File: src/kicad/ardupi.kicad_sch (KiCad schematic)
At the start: 64 parts, among them J1 RPI-4B-Header, J10 Conn_01x04, J11 TSW-108-08-L-T-RA, J2 Conn_01x10, J3 Conn_01x05, J4 Conn_01x04, J6 Conn_01x05, J7 Conn_01x06, J8 Conn_01x04, J9 Conn_01x02, U1 CAT24C256HU4IGT3, U2 ULN2803ADWR, U3 PCA9685PW, U4 ADS1115IDGSR, U5 MPU-9250, U6 BMP280

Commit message: add CAT24C32WI-GT3
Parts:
- removed JP2: ID_WP, Ardupi:SOLDERJUMPER_REFLOW_NOPASTE, symbol Jumper:SolderJumper_2_Open
- removed U1: CAT24C256HU4IGT3, Ardupi:CAT24C256HU4IGT3, symbol ArduPi:CAT24C256HU4IGT3
- added R3: 1k, Resistor_SMD:R_0402_1005Metric, symbol Device:R_Small
- added SJ_A7: SOLDERJUMPERREFLOW_NOPASTE, Ardupi:SOLDERJUMPER_REFLOW_NOPASTE, symbol ArduPi:SOLDERJUMPERREFLOW_NOPASTE
- added U1: CAT24C32WI-GT3, Ardupi:CAT24C32WI-GT3, symbol ArduPi:CAT24C32WI-GT3
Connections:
- net ID_SDA is gone; now on net ID_SD: R21.1
- net +3V3: now also J1.1 (+3.3V), J1.17 (+3.3V), R3.2, U1.8 (VCC)
- net GND: now also J1.25 (GND), J1.39 (GND), J1.9 (GND), SJ_A7.1, U1.1 (A0), U1.2 (A1), U1.3 (A2), U1.4 (VSS)
- net LED1: now also J1.13 (GPIO27)
- net LED2: now also J1.15 (GPIO22)
- net LED3: now also J1.7 (GPIO4)
- net RC1: now also J1.29 (GPIO5)
- net RC2: now also J1.31 (GPIO6)
- net RC3: now also J1.33 (GPIO13)
- net RC4: now also J1.35 (GPIO_19)
- net RC5: now also J1.37 (GPIO26)
- net SCL1: now also J1.5 (GPIO3)
- net SDA1: now also J1.3 (GPIO2)
- net SPI_MISO: now also J1.21 (GPIO9)
- net SPI_MOSI: now also J1.19 (GPIO10)
- net SPI_SCLK: now also J1.23 (GPIO11)
- net SRVO_EN: now also J1.11 (GPIO17)
- net ID_SD: now reaches J1.27 (Reserved)
- net ID_SD: now also U1.5 (SDA)
- net ID_SCL renamed ID_SC
- net ID_SC: now also U1.6 (SCL)
- new net: R3.1, SJ_A7.2, U1.7 (WP)
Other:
- moved on the sheet: C4, C5, C9, C_PCA1, J1, J10, J11, J2, J3, J4, J6, J7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

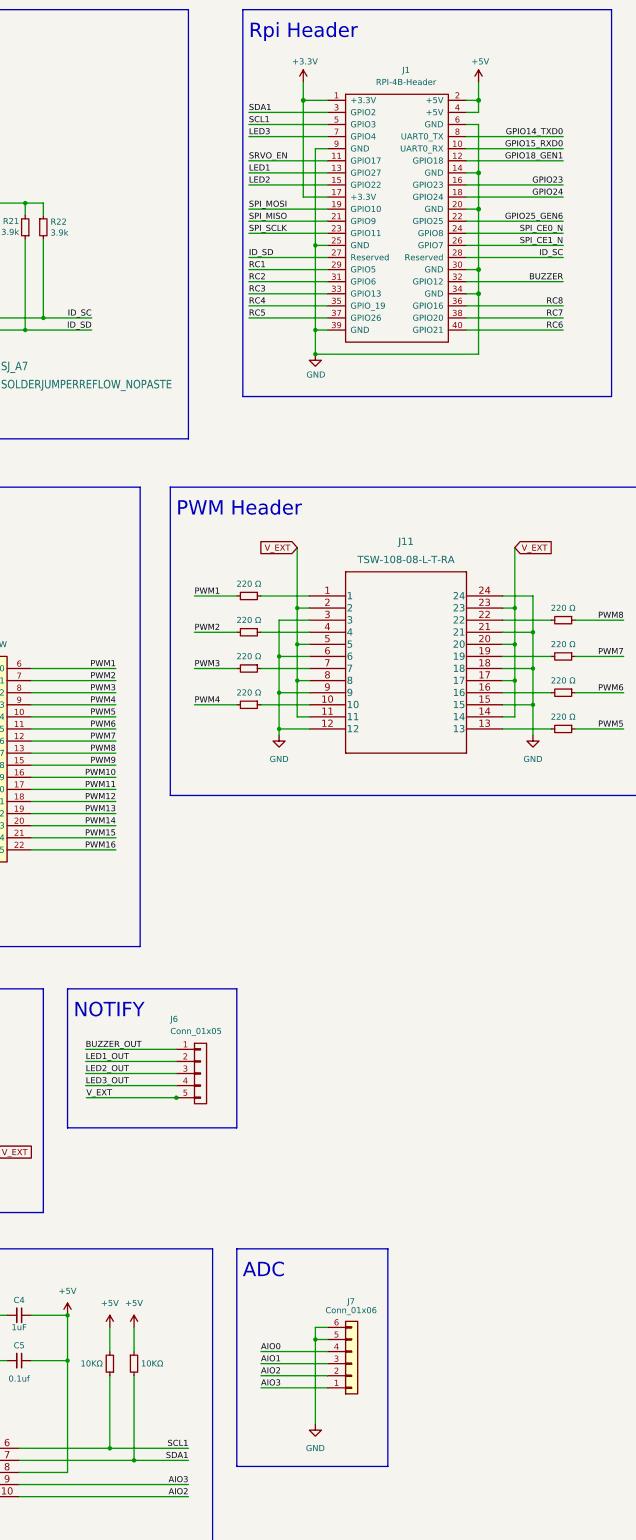
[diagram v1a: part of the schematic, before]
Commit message: define PWM header pin table.
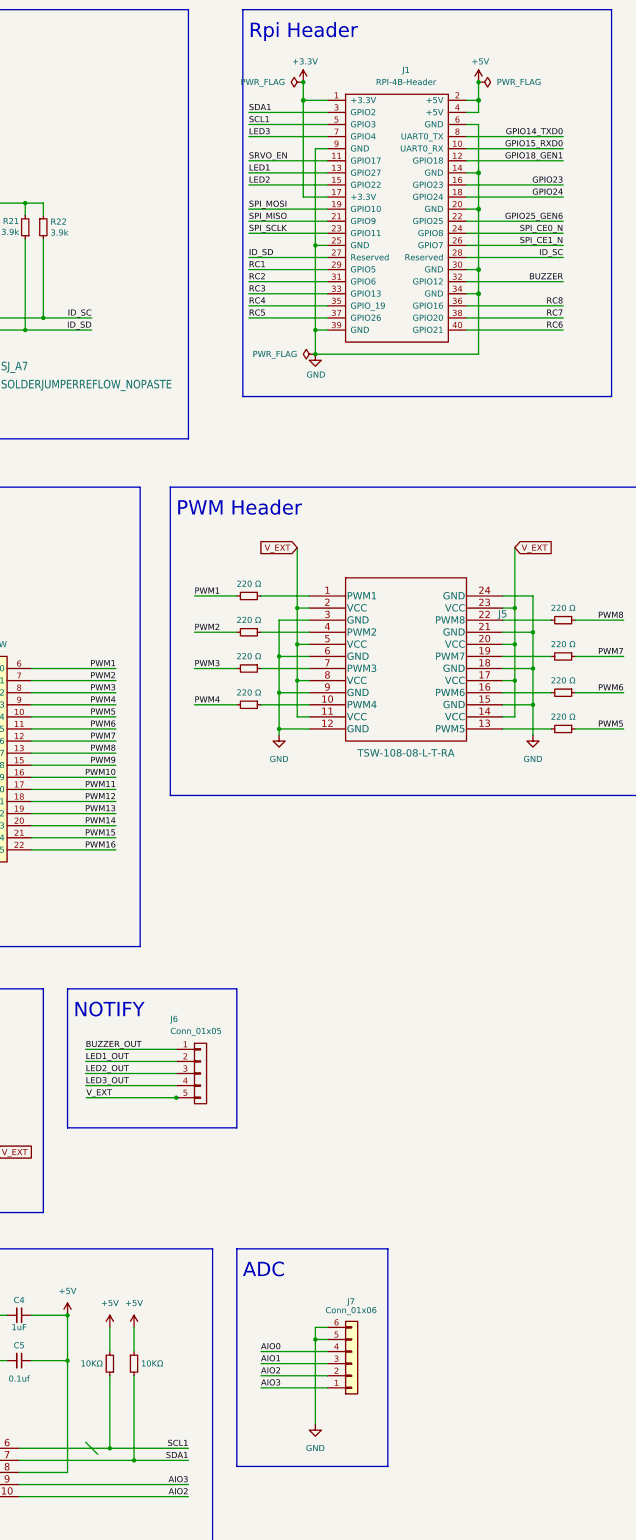
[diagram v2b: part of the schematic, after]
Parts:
- removed J11: TSW-108-08-L-T-RA, Ardupi:TSW-108-08-L-T-RA, symbol ardupi:TSW-108-08-L-T-RA
- added J5: TSW-108-08-L-T-RA, TSW-108-08-T-T-RA_SAI, symbol ArduPi:TSW-108-08-L-T-RA
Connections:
- net GND: now also J5.12 (GND), J5.15 (GND), J5.18 (GND), J5.21 (GND), J5.24 (GND), J5.3 (GND), J5.6 (GND), J5.9 (GND)
- net V_EXT: now also J5.11 (VCC), J5.14 (VCC), J5.17 (VCC), J5.2 (VCC), J5.20 (VCC), J5.23 (VCC), J5.5 (VCC), J5.8 (VCC)
- net at R20.2: now also J5.13 (PWM5)
- net at R14.1: now also J5.4 (PWM2)
- net at R16.1: now also J5.10 (PWM4)
- net at R19.2: now also J5.16 (PWM6)
- net at R18.2: now also J5.19 (PWM7)
- net at R13.1: now also J5.1 (PWM1)
- net at R17.2: now also J5.22 (PWM8)
- net at R15.1: now also J5.7 (PWM3)

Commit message: +NEO-M8Q-01A module
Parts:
- removed J10: Conn_01x04, Connector_JST:JST_EH_B4B-EH-A_1x04_P2.50mm_Vertical, symbol Connector_Generic:Conn_01x04
- added M1: NEO-M8Q-01A, Ardupi:ublox_NEO, symbol ArduPi:NEO-M8Q-01A
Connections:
- net GND: now also M1.10 (GND), M1.12 (GND), M1.13 (GND), M1.24 (GND)
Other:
- note added: "GPS"
- note removed: "COMPASS"

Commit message: + expresslrs.
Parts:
- added U7: RFM95W-868S2, Ardupi:RFM95W-868S2, symbol ArduPi:RFM95W-868S2
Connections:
- net +3V3: now also U7.13 (3_3V)
- net GND: now also U7.1 (GND), U7.10 (GND@2), U7.8 (GND@1)
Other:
- note added: "Barometer"
- note added: "ExpressLRS"
- note added: "ExpressLRS Antenna"
- note added: "GPS Antenna"
- note added: "IMU"
- note added: "LED,Buzzer"
- note added: "PWM"
- note added: "RPI Header"
- note removed: "ADS1115IDGSR ADC"
- note removed: "BMP280 Barometer"
- note removed: "ID_SD and ID_SC PINS: These pins are reserved for HAT ID EEPROM. At boot time this I2C interface will be interrogated to look for an EEPROM that identifes the attached board and allows automagic setup of the GPIOs (and optionally, Linux drivers). Bridging JP1 enables write protection. DO NOT USE these pins for anything other than attaching an I2C ID EEPROM. Leave unconnected if ID EEPROM not requ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"
- note removed: "MPU9250 IMU"
- note removed: "PCA9685 PWM"
- note removed: "Rpi Header"
- note removed: "ULN2803 LED,BUZZER"
- moved on the sheet: C2, C3, C4, C5, C6, C7, C8, C9, C_PCA1, J1, J2, J3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

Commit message: fix
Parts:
- renumbered U7 to M2
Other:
- note added: "Power Manangement"
- moved on the sheet: C2, C3, C6, C7, C8, J9, R11, R12, U5, U6

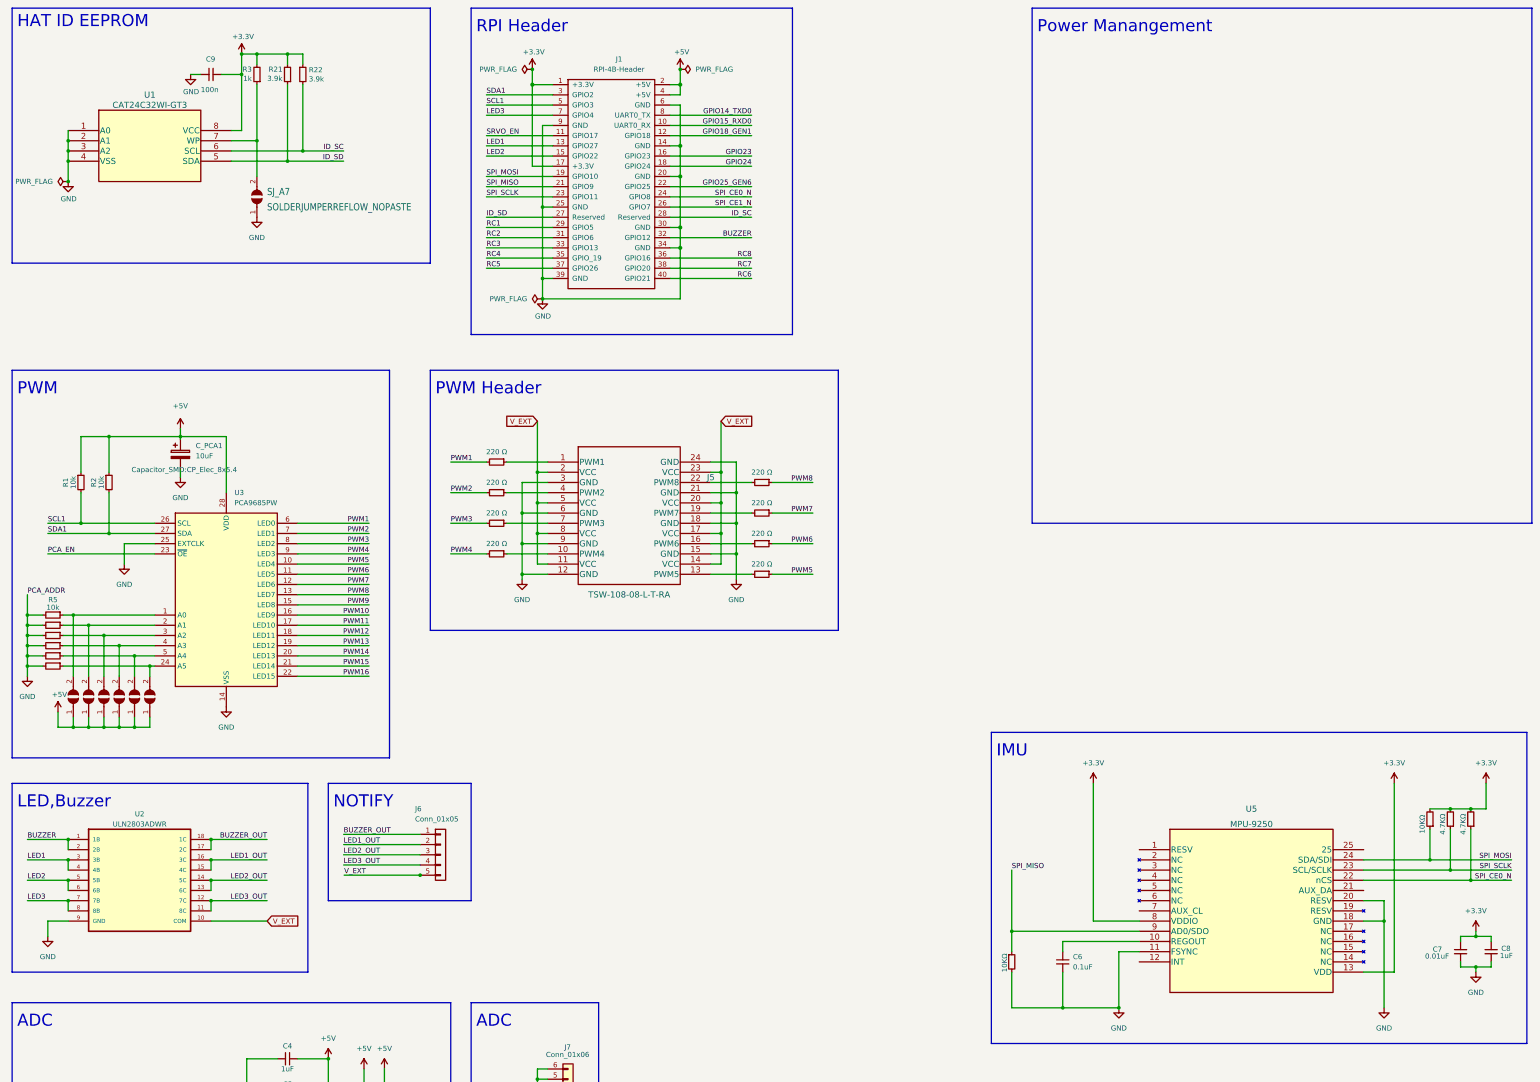
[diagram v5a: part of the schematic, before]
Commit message: elec: 9250 and remove a label between gnd & v
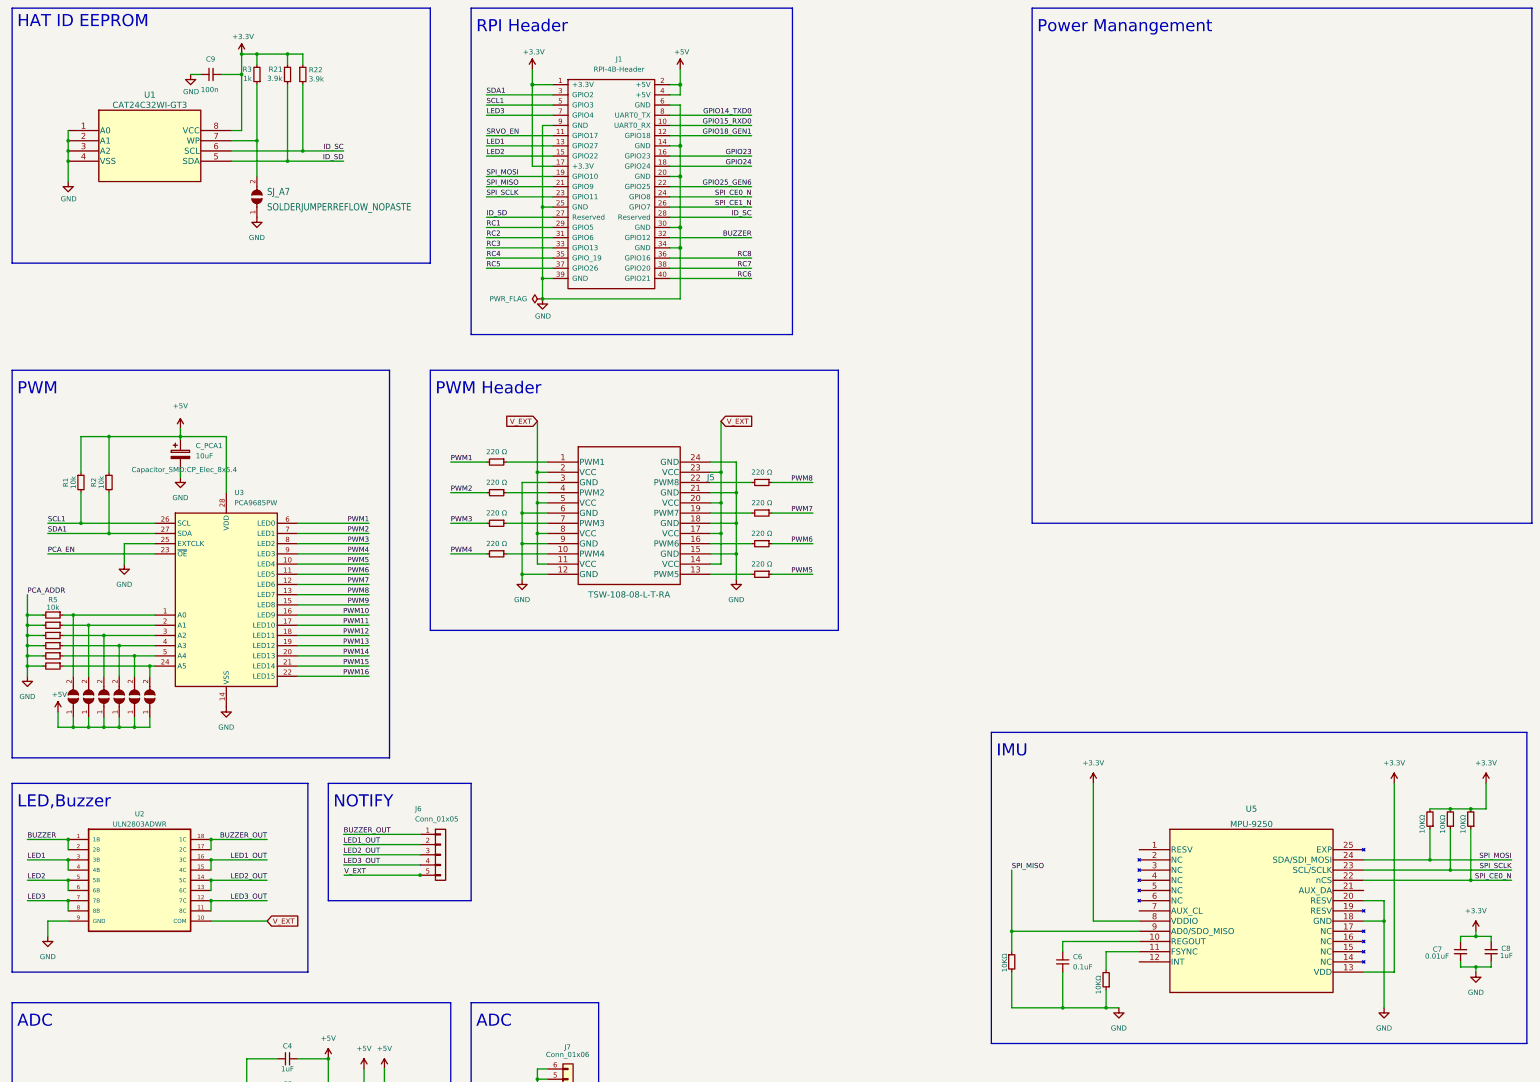
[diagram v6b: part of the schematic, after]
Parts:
- added R?: 10KΩ, Resistor_SMD:R_0402_1005Metric, symbol Device:R_Small
- R29, R30: value 4.7KΩ -> 10KΩ
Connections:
- net GND: now also R?.1; no longer U5.11 (FSYNC)
- new net: R?.2, U5.11 (FSYNC)
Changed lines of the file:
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@@
   (junction (at 386.08 222.25) (diameter 0) (color 0 0 0 0)
   )
-  (junction (at 152.4 38.1) (diameter 0) (color 0 0 0 0)
-  )
   (junction (at 57.15 186.69) (diameter 0) (color 0 0 0 0)
   )
@@
   (junction (at 154.94 95.25) (diameter 0) (color 0 0 0 0)
   )
-  (junction (at 36.83 66.04) (diameter 0) (color 0 0 0 0)
-  )
   (junction (at 26.67 186.69) (diameter 0) (color 0 0 0 0)
   )
@@
   (junction (at 91.44 34.29) (diameter 0) (color 0 0 0 0)
   )
-  (junction (at 298.45 271.78) (diameter 0) (color 0 0 0 0)
-  )
   (junction (at 46.99 153.67) (diameter 0) (color 0 0 0 0)
   )
@@
   (junction (at 80.01 34.29) (diameter 0) (color 0 0 0 0)
   )
-  (junction (at 189.23 38.1) (diameter 0) (color 0 0 0 0)
-  )
   (junction (at 368.3 306.07) (diameter 0) (color 0 0 0 0)
   )
   (junction (at 318.77 323.85) (diameter 0) (color 0 0 0 0)
   )
+  (junction (at 295.275 271.78) (diameter 0) (color 0 0 0 0)
+  )
   (junction (at 36.83 245.11) (diameter 0) (color 0 0 0 0)
   )
@@
     (stroke (width 0) (type default) (color 0 0 0 0))
   )
-  (wire (pts (xy 303.53 257.81) (xy 298.45 257.81))
+  (wire (pts (xy 295.275 257.81) (xy 303.53 257.81))
     (stroke (width 0) (type default) (color 0 0 0 0))
   )
@@
     (stroke (width 0) (type default) (color 0 0 0 0))
   )
+  (wire (pts (xy 295.275 271.78) (xy 298.45 271.78))
+    (stroke (width 0) (type default) (color 0 0 0 0))
+  )
   (wire (pts (xy 64.77 129.54) (xy 64.77 130.175))
     (stroke (width 0) (type default) (color 0 0 0 0))
@@
     (stroke (width 0) (type default) (color 0 0 0 0))
   )
-  (wire (pts (xy 284.48 271.78) (xy 298.45 271.78))
+  (wire (pts (xy 284.48 271.78) (xy 295.275 271.78))
     (stroke (width 0) (type default) (color 0 0 0 0))
   )
@@
     (stroke (width 0) (type default) (color 0 0 0 0))
   )
+  (wire (pts (xy 295.275 267.335) (xy 295.275 271.78))
+    (stroke (width 0) (type default) (color 0 0 0 0))
+  )
   (wire (pts (xy 36.83 53.34) (xy 36.83 55.88))
     (stroke (width 0) (type default) (color 0 0 0 0))
@@
     (stroke (width 0) (type default) (color 0 0 0 0))
   )
-  (wire (pts (xy 298.45 257.81) (xy 298.45 271.78))
-    (stroke (width 0) (type default) (color 0 0 0 0))
-  )
   (wire (pts (xy 35.56 176.53) (xy 41.91 176.53))
     (stroke (width 0) (type default) (color 0 0 0 0))
@@
     (stroke (width 0) (type default) (color 0 0 0 0))
   )
+  (wire (pts (xy 295.275 257.81) (xy 295.275 262.255))
+    (stroke (width 0) (type default) (color 0 0 0 0))
+  )
   (wire (pts (xy 38.1 201.93) (xy 41.91 201.93))
     (stroke (width 0) (type default) (color 0 0 0 0))
@@
     (pin "1")
   )
-  (symbol (lib_id "power:PWR_FLAG") (at 189.23 38.1 270) (unit 1)
-    (in_bom yes) (on_board yes) (fields_autoplaced)
-    (property "Reference" "#FLG04" (id 0) (at 191.135 38.1 0)
-      (effects (font (size 1.27 1.27)) hide)
-    )
-    (property "Value" "PWR_FLAG" (id 1) (at 193.04 38.0999 90)
-      (effects (font (size 1.27 1.27)) (justify left))
-    )
-    (property "Footprint" "" (id 2) (at 189.23 38.1 0)
-      (effects (font (size 1.27 1.27)) hide)
-    )
-    (property "Datasheet" "~" (id 3) (at 189.23 38.1 0)
-      (effects (font (size 1.27 1.27)) hide)
-    )
-    (pin "1")
-  )
   (symbol (lib_id "power:+3.3V") (at 368.3 306.07 0) (unit 1)
     (in_bom yes) (on_board yes) (fields_autoplaced)
@@
     (pin "1")
   )
-  (symbol (lib_id "power:PWR_FLAG") (at 36.83 66.04 90) (unit 1)
-    (in_bom yes) (on_board yes) (fields_autoplaced)
-    (property "Reference" "#FLG01" (id 0) (at 34.925 66.04 0)
-      (effects (font (size 1.27 1.27)) hide)
-    )
-    (property "Value" "PWR_FLAG" (id 1) (at 33.02 66.0399 90)
-      (effects (font (size 1.27 1.27)) (justify left))
-    )
-    (property "Footprint" "" (id 2) (at 36.83 66.04 0)
-      (effects (font (size 1.27 1.27)) hide)
-    )
-    (property "Datasheet" "~" (id 3) (at 36.83 66.04 0)
-      (effects (font (size 1.27 1.27)) hide)
-    )
-    (pin "1")
-  )
   (symbol (lib_id "Device:R_Small") (at 143.51 158.75 270) (unit 1)
     (in_bom yes) (on_board yes)
@@
     (pin "9")
   )
-  (symbol (lib_id "power:PWR_FLAG") (at 152.4 38.1 90) (unit 1)
-    (in_bom yes) (on_board yes) (fields_autoplaced)
-    (property "Reference" "#FLG03" (id 0) (at 150.495 38.1 0)
-      (effects (font (size 1.27 1.27)) hide)
-    )
-    (property "Value" "PWR_FLAG" (id 1) (at 148.59 38.0999 90)
-      (effects (font (size 1.27 1.27)) (justify left))
-    )
-    (property "Footprint" "" (id 2) (at 152.4 38.1 0)
-      (effects (font (size 1.27 1.27)) hide)
-    )
-    (property "Datasheet" "~" (id 3) (at 152.4 38.1 0)
-      (effects (font (size 1.27 1.27)) hide)
-    )
-    (pin "1")
-  )
   (symbol (lib_id "Device:R_Small") (at 33.02 176.53 270) (unit 1)
     (in_bom yes) (on_board yes) (fields_autoplaced)
@@
       (effects (font (size 1.27 1.27)) hide)
     )
-    (property "Value" "4.7KΩ" (id 1) (at 384.175 226.06 90))
+    (property "Value" "10KΩ" (id 1) (at 384.175 226.06 90))
     (property "Footprint" "Resistor_SMD:R_0402_1005Metric" (id 2) (at 389.89 224.79 90)
       (effects (font (size 1.27 1.27)) hide)
@@
     (pin "2")
   )
+  (symbol (lib_id "Device:R_Small") (at 295.275 264.795 180) (unit 1)
+    (in_bom yes) (on_board yes)
+    (property "Reference" "R?" (id 0) (at 293.37 267.97 90)
+      (effects (font (size 1.27 1.27)) hide)
+    )
+    (property "Value" "10KΩ" (id 1) (at 293.37 266.065 90))
+    (property "Footprint" "Resistor_SMD:R_0402_1005Metric" (id 2) (at 299.085 264.795 90)
+      (effects (font (size 1.27 1.27)) hide)
+    )
+    (property "Datasheet" "~" (id 3) (at 295.275 264.795 0)
+      (effects (font (size 1.27 1.27)) hide)
+    )
+    (pin "1")
+    (pin "2")
+  )
   (symbol (lib_id "power:+3.3V") (at 367.03 215.9 0) (unit 1)
     (in_bom yes) (on_board yes) (fields_autoplaced)
@@
       (effects (font (size 1.27 1.27)) hide)
     )
-    (property "Value" "4.7KΩ" (id 1) (at 379.095 226.06 90))
+    (property "Value" "10KΩ" (id 1) (at 379.095 226.06 90))
     (property "Footprint" "Resistor_SMD:R_0402_1005Metric" (id 2) (at 384.81 224.79 90)
       (effects (font (size 1.27 1.27)) hide)
@@
   )
   (symbol_instances
-    (path "/20d1443b-331d-45eb-9283-83c84b2d629f"
-      (reference "#FLG01") (unit 1) (value "PWR_FLAG") (footprint "")
-    )
     (path "/b3d30f20-3604-4f45-917b-900f6ffca4b6"
       (reference "#FLG02") (unit 1) (value "PWR_FLAG") (footprint "")
     )
-    (path "/4d660207-b095-4ded-9a2c-d3d9bc9ae046"
-      (reference "#FLG03") (unit 1) (value "PWR_FLAG") (footprint "")
-    )
-    (path "/11f010e3-a23f-42bd-8bc9-3919e06f8f41"
-      (reference "#FLG04") (unit 1) (value "PWR_FLAG") (footprint "")
-    )
     (path "/0f8bbff2-b444-42b9-8b55-9321ee4eeefd"
       (reference "#PWR01") (unit 1) (value "+3.3V") (footprint "")
@@
     )
     (path "/b39b62c9-1b80-4159-bec7-d94e4ab77297"
-      (reference "R29") (unit 1) (value "4.7KΩ") (footprint "Resistor_SMD:R_0402_1005Metric")
+      (reference "R29") (unit 1) (value "10KΩ") (footprint "Resistor_SMD:R_0402_1005Metric")
     )
     (path "/6cfff18e-a2c8-4d21-a869-d63ae888410c"
-      (reference "R30") (unit 1) (value "4.7KΩ") (footprint "Resistor_SMD:R_0402_1005Metric")
+      (reference "R30") (unit 1) (value "10KΩ") (footprint "Resistor_SMD:R_0402_1005Metric")
     )
     (path "/d7f38428-b5d0-443f-9732-e20c2ab596b8"
@@
       (reference "R36") (unit 1) (value "10KΩ") (footprint "Resistor_SMD:R_0402_1005Metric")
     )
+    (path "/a6fca7e1-abef-405b-98ed-698ba4263c27"
+      (reference "R?") (unit 1) (value "10KΩ") (footprint "Resistor_SMD:R_0402_1005Metric")
+    )
     (path "/58dfd284-23c9-4434-ace3-66b6d8cf5dab"
